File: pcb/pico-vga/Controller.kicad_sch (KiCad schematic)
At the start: 11 parts

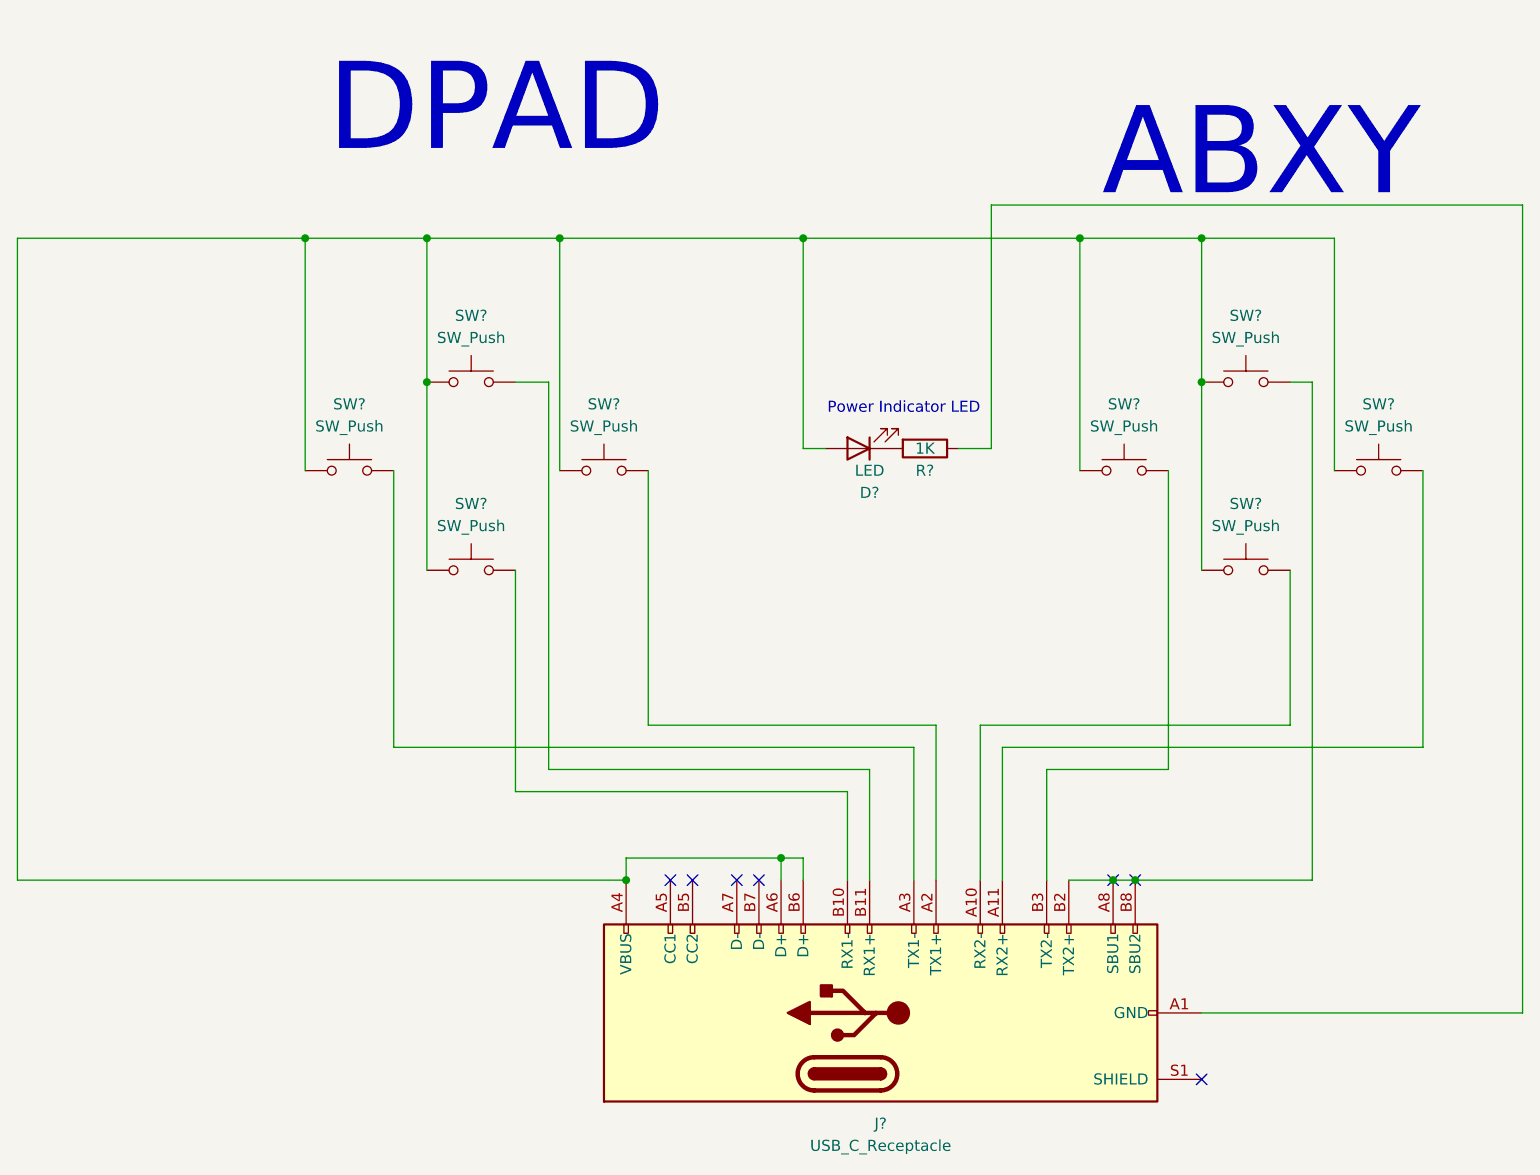
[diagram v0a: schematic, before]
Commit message: schematic completely finished, passes ERC, fully labeled
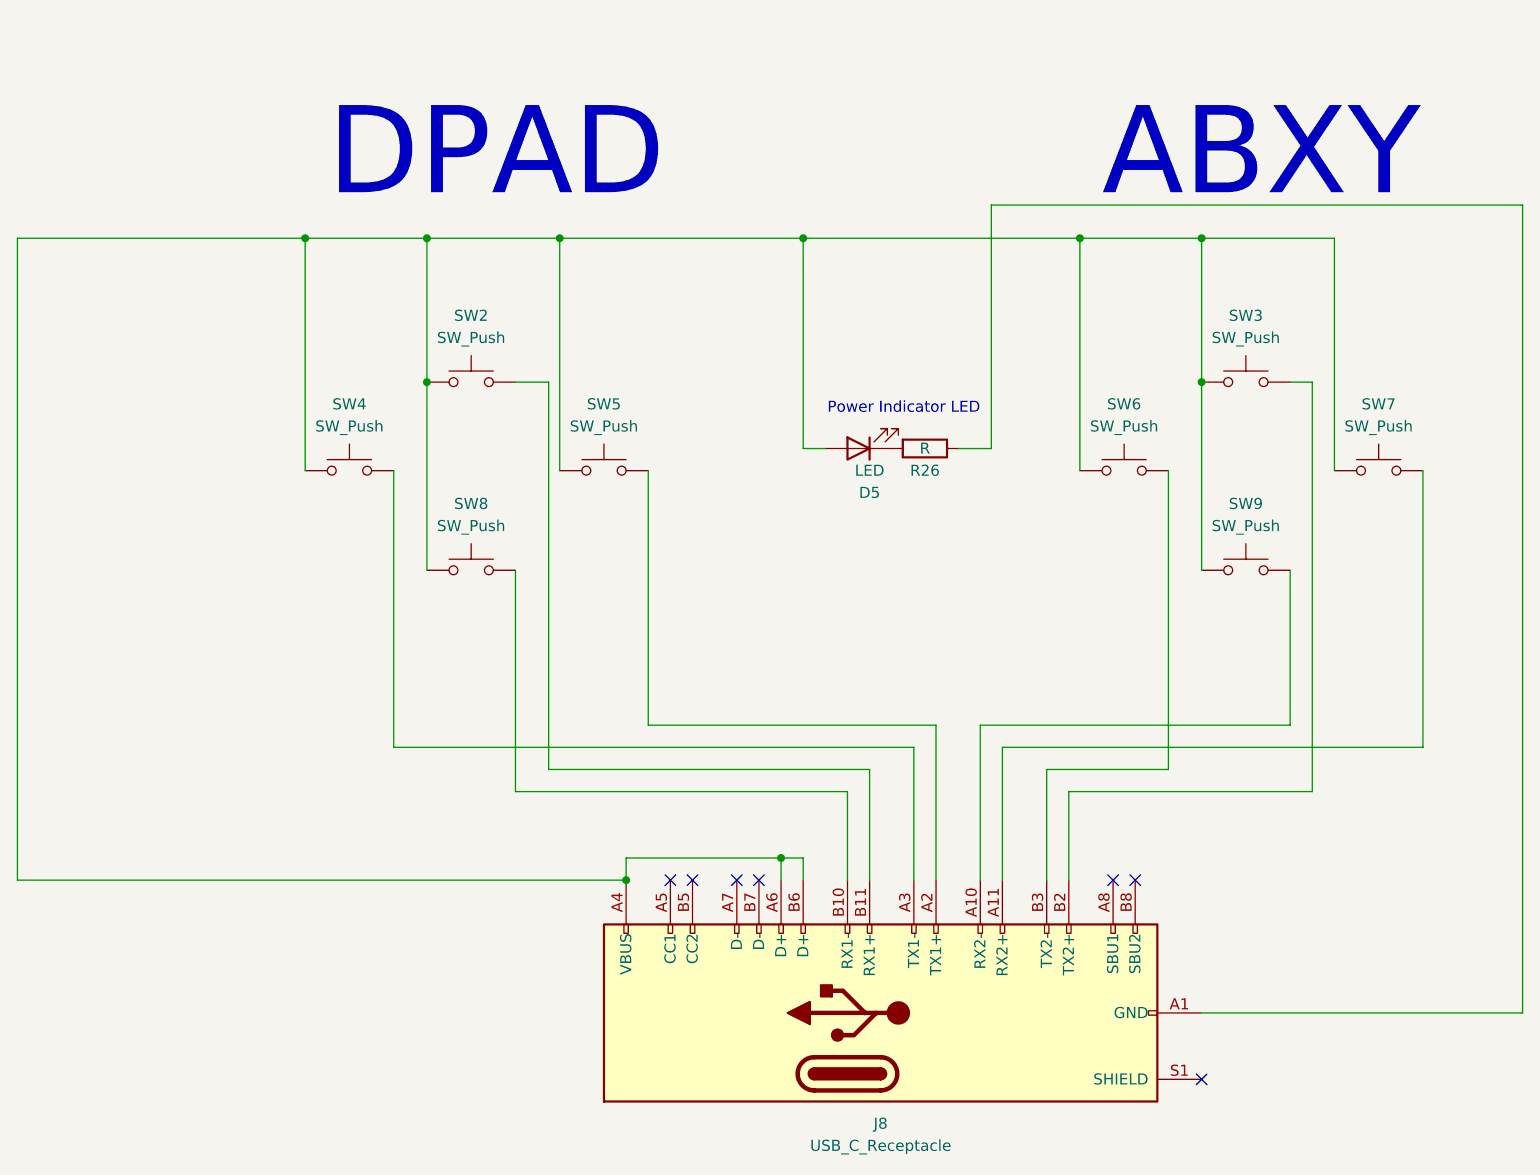
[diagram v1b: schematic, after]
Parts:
- R26: renamed from R?; value 1K -> R
- gave numbers to parts that had none: 10
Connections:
- net at J8.B2 (TX2+), SW3.2: no longer J8.A8 (SBU1), J8.B8 (SBU2)
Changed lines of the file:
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@@
   (junction (at 177.8 81.28) (diameter 0) (color 0 0 0 0)
-  )
-  (junction (at 167.64 138.43) (diameter 0) (color 0 0 0 0)
-  )
-  (junction (at 170.18 138.43) (diameter 0) (color 0 0 0 0)
   )
   (junction (at 132.08 64.77) (diameter 0) (color 0 0 0 0)
@@
   (no_connect (at 124.46 138.43))
   (no_connect (at 167.64 138.43))
+  (no_connect (at 177.8 161.29))
   (no_connect (at 170.18 138.43))
-  (no_connect (at 177.8 161.29))
   (wire (pts (xy 99.06 128.27) (xy 137.16 128.27))
     (stroke (width 0) (type default) (color 0 0 0 0))
   )
-  (wire (pts (xy 162.56 138.43) (xy 167.64 138.43))
-    (stroke (width 0) (type default) (color 0 0 0 0))
-  )
   (wire (pts (xy 129.54 135.89) (xy 111.76 135.89))
     (stroke (width 0) (type default) (color 0 0 0 0))
@@
     (stroke (width 0) (type default) (color 0 0 0 0))
   )
+  (wire (pts (xy 162.56 138.43) (xy 162.56 128.27))
+    (stroke (width 0) (type default) (color 0 0 0 0))
+  )
   (wire (pts (xy 154.94 123.19) (xy 154.94 138.43))
     (stroke (width 0) (type default) (color 0 0 0 0))
@@
     (stroke (width 0) (type default) (color 0 0 0 0))
   )
-  (wire (pts (xy 170.18 138.43) (xy 190.5 138.43))
+  (wire (pts (xy 162.56 128.27) (xy 190.5 128.27))
     (stroke (width 0) (type default) (color 0 0 0 0))
   )
@@
     (stroke (width 0) (type default) (color 0 0 0 0))
   )
-  (wire (pts (xy 190.5 138.43) (xy 190.5 81.28))
+  (wire (pts (xy 190.5 128.27) (xy 190.5 81.28))
     (stroke (width 0) (type default) (color 0 0 0 0))
   )
@@
   )
   (wire (pts (xy 132.08 64.77) (xy 163.83 64.77))
-    (stroke (width 0) (type default) (color 0 0 0 0))
-  )
-  (wire (pts (xy 167.64 138.43) (xy 170.18 138.43))
     (stroke (width 0) (type default) (color 0 0 0 0))
   )
@@
     (effects (font (size 1.27 1.27)) (justify right bottom))
   )
-  (text "DPAD" (at 77.47 55.88 0)
+  (text "DPAD" (at 77.47 60.96 0)
     (effects (font (size 10 10)) (justify left bottom))
   )
@@
   (symbol (lib_id "Connector:USB_C_Receptacle") (at 137.16 153.67 90) (unit 1)
     (in_bom yes) (on_board yes) (fields_autoplaced)
-    (property "Reference" "J?" (id 0) (at 140.97 166.37 90))
+    (property "Reference" "J8" (id 0) (at 140.97 166.37 90))
     (property "Value" "USB_C_Receptacle" (id 1) (at 140.97 168.91 90))
     (property "Footprint" "" (id 2) (at 137.16 149.86 0)
@@
   (symbol (lib_id "Switch:SW_Push") (at 93.98 102.87 0) (unit 1)
     (in_bom yes) (on_board yes) (fields_autoplaced)
-    (property "Reference" "SW?" (id 0) (at 93.98 95.25 0))
+    (property "Reference" "SW8" (id 0) (at 93.98 95.25 0))
     (property "Value" "SW_Push" (id 1) (at 93.98 97.79 0))
     (property "Footprint" "" (id 2) (at 93.98 97.79 0)
@@
   (symbol (lib_id "Switch:SW_Push") (at 182.88 81.28 0) (unit 1)
     (in_bom yes) (on_board yes) (fields_autoplaced)
-    (property "Reference" "SW?" (id 0) (at 182.88 73.66 0))
+    (property "Reference" "SW3" (id 0) (at 182.88 73.66 0))
     (property "Value" "SW_Push" (id 1) (at 182.88 76.2 0))
     (property "Footprint" "" (id 2) (at 182.88 76.2 0)
@@
   (symbol (lib_id "Device:R") (at 146.05 88.9 270) (unit 1)
     (in_bom yes) (on_board yes)
-    (property "Reference" "R?" (id 0) (at 146.05 91.44 90))
-    (property "Value" "1K" (id 1) (at 146.05 88.9 90))
+    (property "Reference" "R26" (id 0) (at 146.05 91.44 90))
+    (property "Value" "R" (id 1) (at 146.05 88.9 90))
     (property "Footprint" "" (id 2) (at 146.05 87.122 90)
       (effects (font (size 1.27 1.27)) hide)
@@
   (symbol (lib_id "Switch:SW_Push") (at 93.98 81.28 0) (unit 1)
     (in_bom yes) (on_board yes) (fields_autoplaced)
-    (property "Reference" "SW?" (id 0) (at 93.98 73.66 0))
+    (property "Reference" "SW2" (id 0) (at 93.98 73.66 0))
     (property "Value" "SW_Push" (id 1) (at 93.98 76.2 0))
     (property "Footprint" "" (id 2) (at 93.98 76.2 0)
@@
   (symbol (lib_id "Switch:SW_Push") (at 198.12 91.44 0) (unit 1)
     (in_bom yes) (on_board yes) (fields_autoplaced)
-    (property "Reference" "SW?" (id 0) (at 198.12 83.82 0))
+    (property "Reference" "SW7" (id 0) (at 198.12 83.82 0))
     (property "Value" "SW_Push" (id 1) (at 198.12 86.36 0))
     (property "Footprint" "" (id 2) (at 198.12 86.36 0)
@@
   (symbol (lib_id "Switch:SW_Push") (at 168.91 91.44 0) (unit 1)
     (in_bom yes) (on_board yes) (fields_autoplaced)
-    (property "Reference" "SW?" (id 0) (at 168.91 83.82 0))
+    (property "Reference" "SW6" (id 0) (at 168.91 83.82 0))
     (property "Value" "SW_Push" (id 1) (at 168.91 86.36 0))
     (property "Footprint" "" (id 2) (at 168.91 86.36 0)
@@
   (symbol (lib_id "Switch:SW_Push") (at 109.22 91.44 0) (unit 1)
     (in_bom yes) (on_board yes) (fields_autoplaced)
-    (property "Reference" "SW?" (id 0) (at 109.22 83.82 0))
+    (property "Reference" "SW5" (id 0) (at 109.22 83.82 0))
     (property "Value" "SW_Push" (id 1) (at 109.22 86.36 0))
     (property "Footprint" "" (id 2) (at 109.22 86.36 0)
@@
   (symbol (lib_id "Device:LED") (at 138.43 88.9 180) (unit 1)
     (in_bom yes) (on_board yes)
-    (property "Reference" "D?" (id 0) (at 139.7 93.98 0))
+    (property "Reference" "D5" (id 0) (at 139.7 93.98 0))
     (property "Value" "LED" (id 1) (at 139.7 91.44 0))
     (property "Footprint" "" (id 2) (at 138.43 88.9 0)
@@
   (symbol (lib_id "Switch:SW_Push") (at 182.88 102.87 0) (unit 1)
     (in_bom yes) (on_board yes) (fields_autoplaced)
-    (property "Reference" "SW?" (id 0) (at 182.88 95.25 0))
+    (property "Reference" "SW9" (id 0) (at 182.88 95.25 0))
     (property "Value" "SW_Push" (id 1) (at 182.88 97.79 0))
     (property "Footprint" "" (id 2) (at 182.88 97.79 0)
@@
   (symbol (lib_id "Switch:SW_Push") (at 80.01 91.44 0) (unit 1)
     (in_bom yes) (on_board yes) (fields_autoplaced)
-    (property "Reference" "SW?" (id 0) (at 80.01 83.82 0))
+    (property "Reference" "SW4" (id 0) (at 80.01 83.82 0))
     (property "Value" "SW_Push" (id 1) (at 80.01 86.36 0))
     (property "Footprint" "" (id 2) (at 80.01 86.36 0)

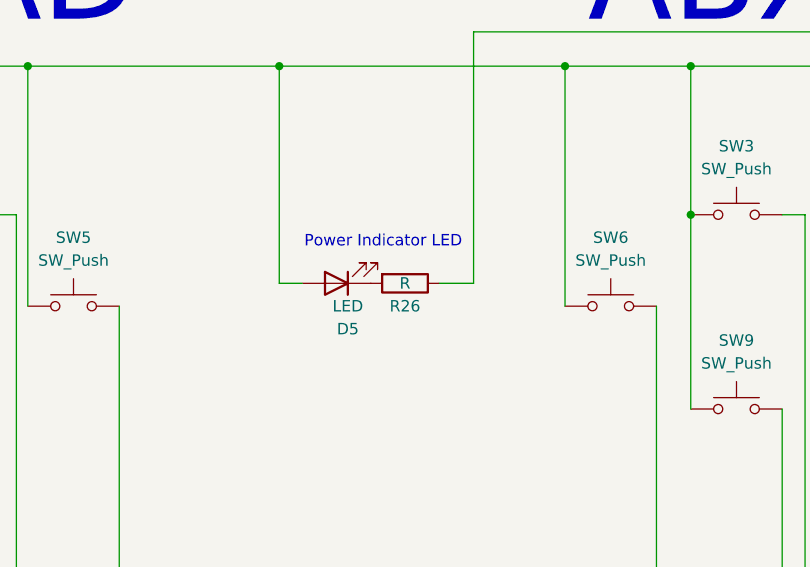
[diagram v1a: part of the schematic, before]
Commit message: NOW it's complete
kicad decided to delete all of my resistor/cap values sometime before the last commit... values are back now, everything's labeled, passes ERC
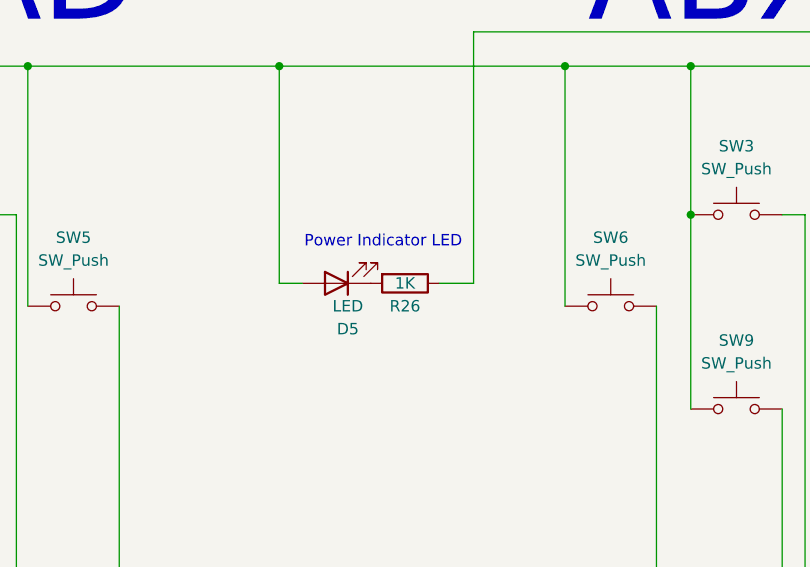
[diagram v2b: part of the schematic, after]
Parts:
- R26: value R -> 1K
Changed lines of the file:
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@@
     (in_bom yes) (on_board yes)
     (property "Reference" "R26" (id 0) (at 146.05 91.44 90))
-    (property "Value" "R" (id 1) (at 146.05 88.9 90))
+    (property "Value" "1K" (id 1) (at 146.05 88.9 90))
     (property "Footprint" "" (id 2) (at 146.05 87.122 90)
       (effects (font (size 1.27 1.27)) hide)

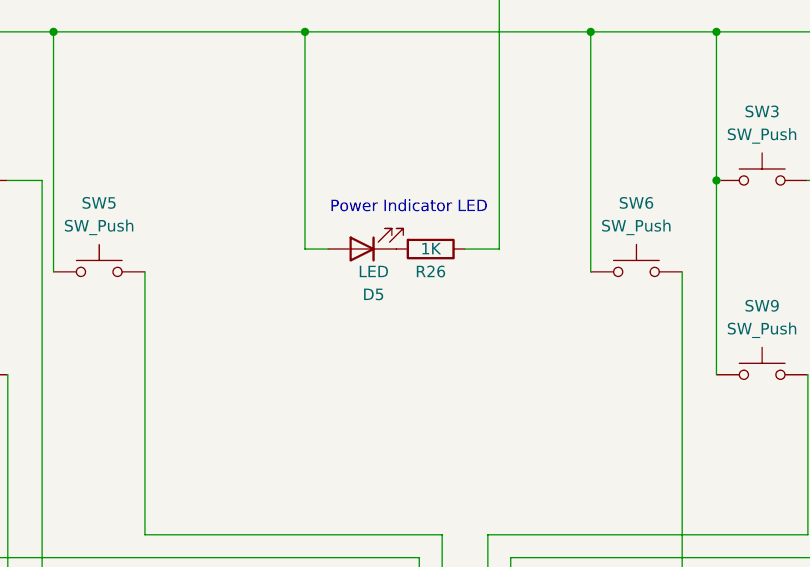
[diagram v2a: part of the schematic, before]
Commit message: pico-vga PCB DONE!!!!
It took many hours of work, and many headaches, but the board is finally done. It passes DRC, everything looks good.
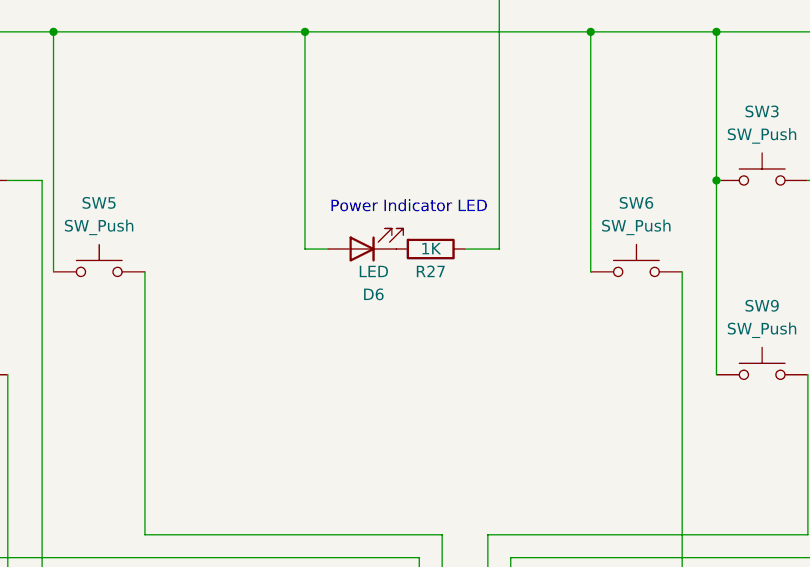
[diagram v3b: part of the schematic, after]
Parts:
- D6: renamed from D5; footprint (none) -> LED_SMD:LED_0805_2012Metric_Pad1.15x1.40mm_HandSolder
- J8: footprint (none) -> pico-vga:USB_C_Receptacle_Molex_2171830001
- R27: renamed from R26; footprint (none) -> Resistor_SMD:R_0603_1608Metric_Pad0.98x0.95mm_HandSolder
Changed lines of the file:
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@@
     (property "Reference" "J8" (id 0) (at 140.97 166.37 90))
     (property "Value" "USB_C_Receptacle" (id 1) (at 140.97 168.91 90))
-    (property "Footprint" "" (id 2) (at 137.16 149.86 0)
+    (property "Footprint" "pico-vga:USB_C_Receptacle_Molex_2171830001" (id 2) (at 137.16 149.86 0)
       (effects (font (size 1.27 1.27)) hide)
     )
@@
   (symbol (lib_id "Device:R") (at 146.05 88.9 270) (unit 1)
     (in_bom yes) (on_board yes)
-    (property "Reference" "R26" (id 0) (at 146.05 91.44 90))
+    (property "Reference" "R27" (id 0) (at 146.05 91.44 90))
     (property "Value" "1K" (id 1) (at 146.05 88.9 90))
-    (property "Footprint" "" (id 2) (at 146.05 87.122 90)
+    (property "Footprint" "Resistor_SMD:R_0603_1608Metric_Pad0.98x0.95mm_HandSolder" (id 2) (at 146.05 87.122 90)
       (effects (font (size 1.27 1.27)) hide)
     )
@@
   (symbol (lib_id "Device:LED") (at 138.43 88.9 180) (unit 1)
     (in_bom yes) (on_board yes)
-    (property "Reference" "D5" (id 0) (at 139.7 93.98 0))
+    (property "Reference" "D6" (id 0) (at 139.7 93.98 0))
     (property "Value" "LED" (id 1) (at 139.7 91.44 0))
-    (property "Footprint" "" (id 2) (at 138.43 88.9 0)
+    (property "Footprint" "LED_SMD:LED_0805_2012Metric_Pad1.15x1.40mm_HandSolder" (id 2) (at 138.43 88.9 0)
       (effects (font (size 1.27 1.27)) hide)
     )

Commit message: Pico-VGA and Controller PCBs DONE!
Updates to pico-vga: I don't remember.... Uhhh.... I did stuff? Whatever, I like the layout, it passes DRC, it's badged, and it now has mounting holes. Updates to controller: It now exists. It also passes DRC, now has rounded corners, and has mounting holes. I'm using custom combination THT/SMD footprints for the buttons, so you can use either one depending on what you buy
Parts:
- removed D6: LED, LED_SMD:LED_0805_2012Metric_Pad1.15x1.40mm_HandSolder, symbol Device:LED
- removed J8: USB_C_Receptacle, pico-vga:USB_C_Receptacle_Molex_2171830001, symbol Connector:USB_C_Receptacle
- removed R27: 1K, Resistor_SMD:R_0603_1608Metric_Pad0.98x0.95mm_HandSolder, symbol Device:R
- removed SW2, SW3, SW4, SW5, SW6, SW7, SW8, SW9: SW_Push, symbol Switch:SW_Push
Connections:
- no-connect marks 7 -> 0
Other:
- note removed: "ABXY"
- note removed: "DPAD"
- note removed: "Power Indicator LED"
